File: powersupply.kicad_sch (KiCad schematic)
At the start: 46 parts, among them J1 5 Pin 3.5mm, U11 LM2596S-12, U3 AMS1117-5.0

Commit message: routed version
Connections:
- net Vdrive renamed VPP
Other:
- moved on the sheet: F6

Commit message: snap
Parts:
- added J9 (x2): Conn_01x06_Male, Connector_PinHeader_2.54mm:PinHeader_1x06_P2.54mm_Vertical, symbol Connector:Conn_01x06_Pin
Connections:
- net +3V3: now also J9.5 (Pin_5), J9.5 (Pin_5)
- net GND: now also J9.6 (Pin_6), J9.6 (Pin_6)
- net VCC: now also J9.3 (Pin_3), J9.3 (Pin_3)
- net VCCQ: now also J9.4 (Pin_4), J9.4 (Pin_4)
- net VDC: now also J9.2 (Pin_2), J9.2 (Pin_2)

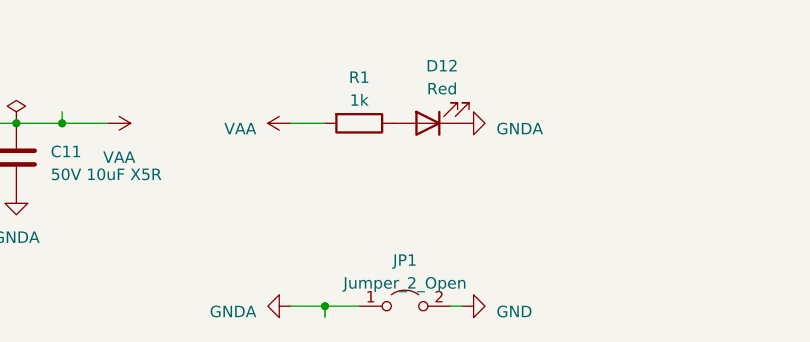
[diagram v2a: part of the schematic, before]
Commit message: Preparation for future use.
Reworked to use i2c bus expanders.
added sketch for add-on boards.
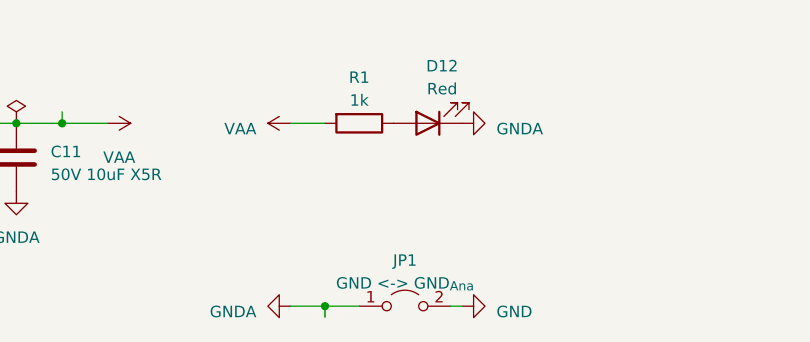
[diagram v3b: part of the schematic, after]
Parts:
- JP1: value Jumper_2_Open -> GND <-> GND_{Ana}
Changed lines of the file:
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@@
       (effects (font (size 1.27 1.27)))
     )
-    (property "Value" "Jumper_2_Open" (at 107.95 180.34 0)
+    (property "Value" "GND <-> GND_{Ana}" (at 107.95 180.34 0)
       (effects (font (size 1.27 1.27)))
     )
